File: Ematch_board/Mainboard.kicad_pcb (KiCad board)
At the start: 4 copper layers, 57.3 x 53.3 mm, 125 parts, among them J1 Conn_01x02_Male, J10 Conn_01x02_Male, J11 Conn_Coaxial, J2 Conn_01x02_Male, J3 Conn_01x02_Male, J4 Conn_01x02_Male, J5 Conn_01x02_Male, J6 Conn_01x02_Male, J7 RBUS, J8 USB_C_Receptacle_USB2.0, J9 Conn_01x02_Male, Q1 MMDT2222A, Q51 PMV20ENR, Q52 PMV20ENR, Q53 PMV20ENR, Q54 PMV20ENR, Q55 PMV20ENR, Q56 PMV20ENR, U1 LTV-247, U2 LTC4411, U3 RT9025-25GSP, U4 LTC4411, U5 SN65HVD230, U6 CP2102-GMR-QFN28

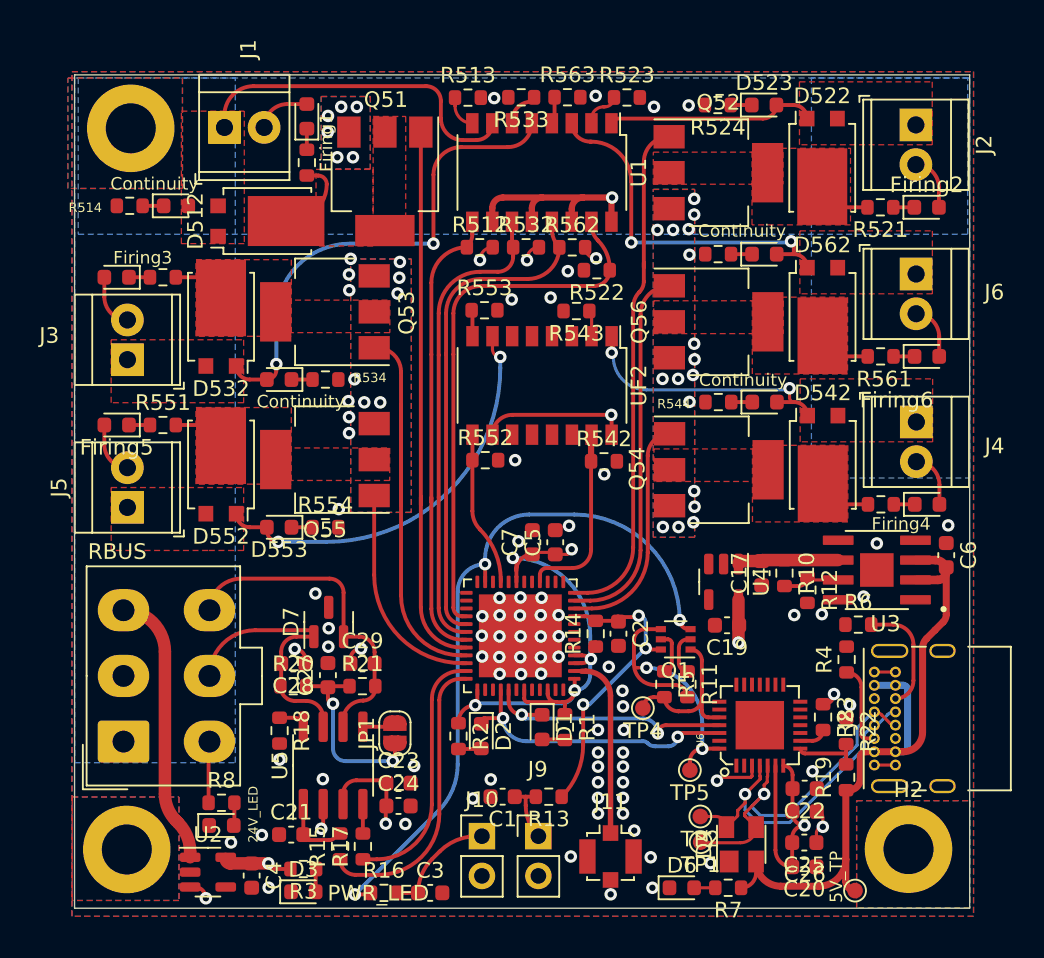
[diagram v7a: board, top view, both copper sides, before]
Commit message: Made front silkscreen intelligible
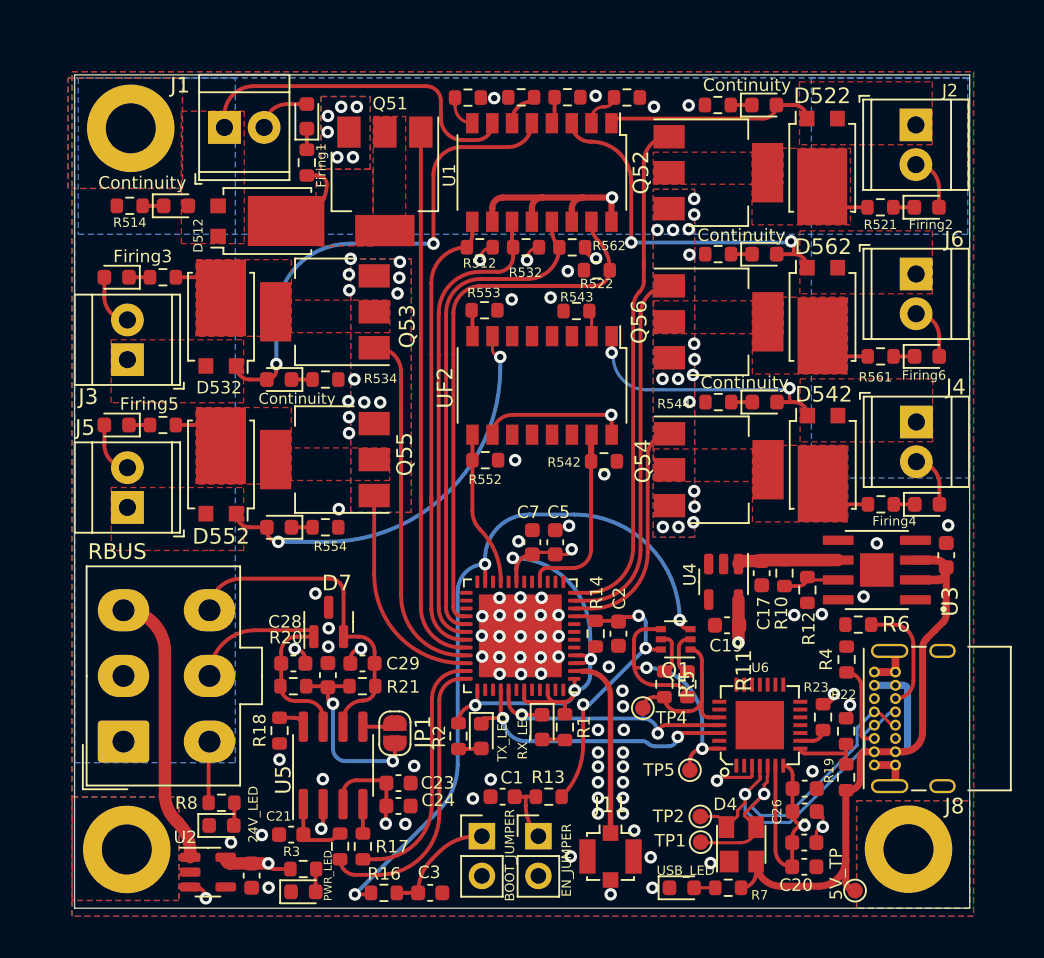
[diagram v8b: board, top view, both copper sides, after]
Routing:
- net GND: track 18.4 -> 21.4 mm
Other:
- board text added: "BOOT_JUMPER"
- board text added: "Continuity"
- board text added: "EN_JUMPER"
